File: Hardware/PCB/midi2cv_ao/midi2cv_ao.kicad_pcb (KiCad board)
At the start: 2 copper layers, 126 x 111 mm, 61 parts, among them IC1 H11L1, IC2 TL074, IC3 TL074, J1 Conn_01x03, J10 AudioJack2, J11 AudioJack2, J12 AudioJack2, J13 AudioJack2, J14 AudioJack2, J15 AudioJack2, J16 AudioJack2, J17 Conn_01x03, J2 Synth_power_2x5, J3 Conn_01x06, J4 Conn_01x10, J8 Conn_01x10, J9 AudioJack2

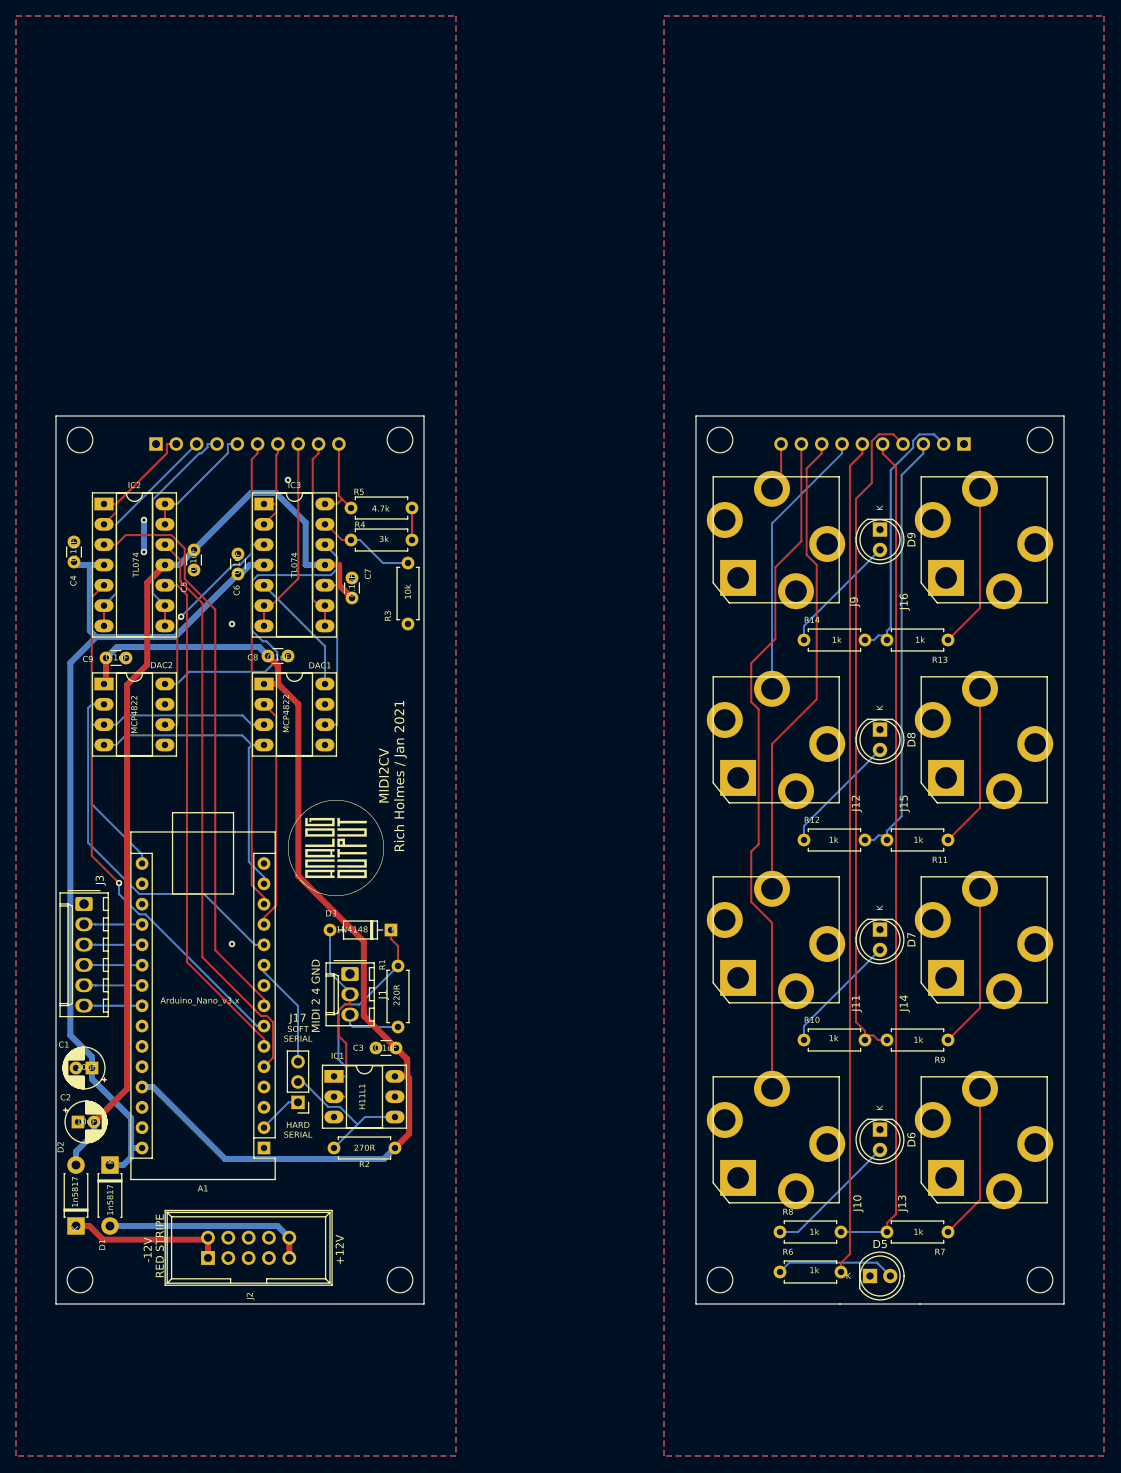
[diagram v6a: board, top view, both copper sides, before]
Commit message: Changed optoisolator, new layout
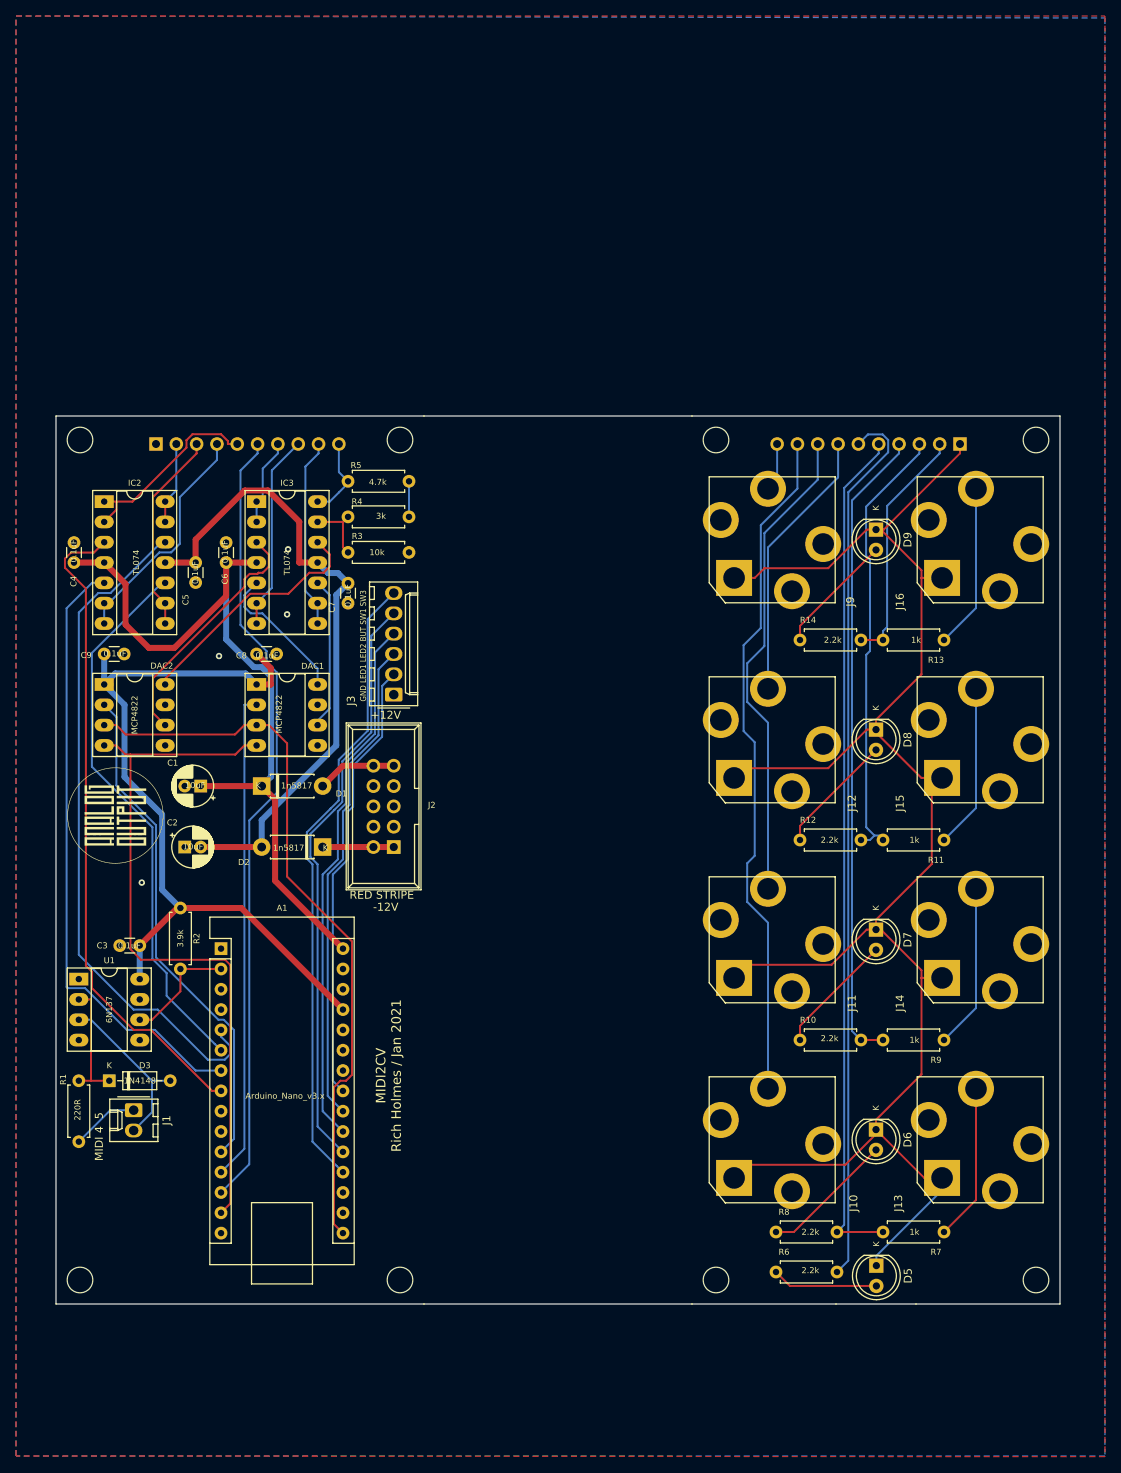
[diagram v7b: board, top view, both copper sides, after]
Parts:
- removed IC1: H11L1, ao_tht:DIP-6_W7.62mm_Socket_LongPads
- removed J17: Conn_01x03, Connector_PinHeader_2.54mm:PinHeader_1x03_P2.54mm_Vertical
- added U1: 6N137, ao_tht:DIP-8_W7.62mm_Socket_LongPads, F.Cu at (42.4, 134.4)
- J1: value Conn_01x03 -> Conn_01x02; footprint Connector_Molex:Molex_KK-254_AE-6410-03A_1x03_P2.54mm_Vertical -> Connector_Molex:Molex_KK-254_AE-6410-02A_1x02_P2.54mm_Vertical
- R10, R12, R14, R6, R8: value 1k -> 2.2k
- R2: value 270R -> 3.9k
- moved D2 56.5 mm to (72.8, 117.9), turned to 180 degrees
- moved J2 56.4 mm to (81.7, 117.9), turned to 180 degrees
- moved D1 51.0 mm to (65.2, 110.3), turned to 0 degrees
- moved J3 46.7 mm to (81.7, 98.8), turned to 90 degrees
- moved R1 42.4 mm to (42.4, 147.1)
- moved R2 40.2 mm to (55.0, 125.5), turned to 270 degrees
- moved D3 39.9 mm to (46.2, 147.1), turned to 0 degrees
- moved C1 37.8 mm to (57.6, 110.3)
- moved C2 36.9 mm to (55.6, 117.9)
- moved C3 34.5 mm to (47.5, 130.2)
- moved J1 32.0 mm to (49.2, 150.8)
- moved G***1 27.9 mm to (46.9, 113.9)
- moved A1 25.5 mm to (60.1, 130.6), turned to 0 degrees
- moved G***2 9.50 mm to (142.0, 107.0)
- moved R3 8.95 mm to (83.6, 81.0), turned to 180 degrees
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- renumbered G***1 to G***2
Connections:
- net /MIDI4 renamed /MIDIPIN5
- A1 pad 10: /SOFT_RX -> Net-(A1-Pad10)
- D5 pad 1: (no net) -> GND1
- D5 pad 2: (no net) -> Net-(D5-Pad2)
- D6 pad 1: (no net) -> GND1
- D6 pad 2: (no net) -> Net-(D6-Pad2)
- D7 pad 1: (no net) -> GND1
- D7 pad 2: (no net) -> Net-(D7-Pad2)
- D8 pad 1: (no net) -> GND1
- D8 pad 2: (no net) -> Net-(D8-Pad2)
- D9 pad 1: (no net) -> GND1
- D9 pad 2: (no net) -> Net-(D9-Pad2)
- IC2 pad 1: /GATE_A -> /CLOCK_4_A
- IC2 pad 13: /CLOCK_4_A -> /GATE_A
- IC2 pad 14: /CLOCK_4_A -> /GATE_A
- IC2 pad 2: /GATE_A -> /CLOCK_4_A
- IC2 pad 6: /TRIGGER_A -> /CLOCK_A
- IC2 pad 7: /TRIGGER_A -> /CLOCK_A
- IC2 pad 8: /CLOCK_A -> /TRIGGER_A
- IC2 pad 9: /CLOCK_A -> /TRIGGER_A
- J1 pad 1: GND -> /MIDIPIN4
- J10 pad S: (no net) -> GND1
- J10 pad T: (no net) -> /Panel components/CONTROL
- J11 pad S: (no net) -> GND1
- J11 pad T: (no net) -> /Panel components/PITCH_BEND
- J12 pad S: (no net) -> GND1
- J12 pad T: (no net) -> /Panel components/VELOCITY
- J13 pad S: (no net) -> GND1
- J13 pad T: (no net) -> /Panel components/CLOCK_4
- J14 pad S: (no net) -> GND1
- J14 pad T: (no net) -> /Panel components/CLOCK
- J15 pad S: (no net) -> GND1
- J15 pad T: (no net) -> /Panel components/TRIGGER
- J16 pad S: (no net) -> GND1
- J16 pad T: (no net) -> /Panel components/GATE
- J3 pad 2: /SW3 -> /PROG_LED2
- J3 pad 3: /SW1 -> /PROG_LED1
- J3 pad 5: /PROG_LED1 -> /SW1
- J3 pad 6: /PROG_LED2 -> /SW3
- J8 pad 1: (no net) -> GND1
- J8 pad 10: (no net) -> /Panel components/NOTE
- J8 pad 2: (no net) -> Net-(J8-Pad2)
- J8 pad 3: (no net) -> Net-(J8-Pad3)
- J8 pad 4: (no net) -> Net-(J8-Pad4)
- J8 pad 5: (no net) -> Net-(J8-Pad5)
- J8 pad 6: (no net) -> Net-(J8-Pad6)
- J8 pad 7: (no net) -> /Panel components/VELOCITY
- J8 pad 8: (no net) -> /Panel components/PITCH_BEND
- J8 pad 9: (no net) -> /Panel components/CONTROL
- J9 pad S: (no net) -> GND1
- J9 pad T: (no net) -> /Panel components/NOTE
- R1 pad 2: /MIDI2 -> /MIDIPIN4
- R10 pad 1: (no net) -> Net-(D7-Pad2)
- R10 pad 2: (no net) -> Net-(J8-Pad4)
- R11 pad 1: (no net) -> /Panel components/TRIGGER
- R11 pad 2: (no net) -> Net-(J8-Pad3)
- R12 pad 1: (no net) -> Net-(D8-Pad2)
- R12 pad 2: (no net) -> Net-(J8-Pad3)
- R13 pad 1: (no net) -> /Panel components/GATE
- R13 pad 2: (no net) -> Net-(J8-Pad2)
- R14 pad 1: (no net) -> Net-(D9-Pad2)
- R14 pad 2: (no net) -> Net-(J8-Pad2)
- R2 pad 2: /RX_J -> /RX0
- R6 pad 1: (no net) -> Net-(D5-Pad2)
- R6 pad 2: (no net) -> Net-(J8-Pad6)
- R7 pad 1: (no net) -> /Panel components/CLOCK_4
- R7 pad 2: (no net) -> Net-(J8-Pad5)
- R8 pad 1: (no net) -> Net-(D6-Pad2)
- R8 pad 2: (no net) -> Net-(J8-Pad5)
- R9 pad 1: (no net) -> /Panel components/CLOCK
- R9 pad 2: (no net) -> Net-(J8-Pad4)
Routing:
- net (no net): track 725.3 -> 0.00 mm
- net GND1: track 0.00 -> 220.2 mm
- net Net-(J8-Pad6): track 0.00 -> 111.2 mm
- net Net-(J8-Pad5): track 0.00 -> 106.4 mm
- net /Panel components/CONTROL: track 0.00 -> 85.4 mm
- net Net-(J8-Pad4): track 0.00 -> 80.2 mm
- net /SW3: track 7.27 -> 78.8 mm
- net /SW1: track 7.27 -> 73.3 mm
- net /Panel components/PITCH_BEND: track 0.00 -> 60.3 mm
- net /BUT: track 7.27 -> 67.0 mm
- net Net-(J8-Pad3): track 0.00 -> 56.1 mm
- net /PROG_LED1: track 7.27 -> 61.4 mm
- net /SDI: track 39.3 -> 89.1 mm
- net /SCK: track 42.4 -> 91.2 mm
- net /PROG_LED2: track 7.27 -> 55.8 mm
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- removed copper zone on B.Cu, net (none)
- removed copper zone on F.Cu, net (none)
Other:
- board size 126 x 111 mm -> 125.5 x 111 mm
- board text added: "GND LED1 LED2 BUT SW1 SW3"
- board text added: "MIDI 4 5"
- board text removed: "HARD SERIAL"
- board text removed: "MIDI 2 4 GND"
- board text removed: "SOFT SERIAL"
